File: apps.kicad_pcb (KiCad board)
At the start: 2 copper layers, 100 x 36 mm, 68 parts, among them J1 1-776280-1, J2 SWD, J3 UART, J4 Conn_01x04, Q1 AO3400A, U1 STM32F103C8Tx, U2 MCP2551, U3 AMS1117-5.0, U4 AMS1117-3.3, U5 SS49E, U6 SS49E, Y1 8M

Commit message: Changed SS49E footprint and updated to KiCAD 9
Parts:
- U5, U6: footprint Package_TO_SOT_THT:TO-92_Inline -> SS49E:SS49E_TO_92_Inline
- moved R11 4.00 mm to (191.5, 50.8)
- moved R9 4.00 mm to (195.5, 76.0)
- moved C17 2.50 mm to (192.2, 76.7), turned to 0 degrees
- moved C19 2.46 mm to (194.7, 50.0), turned to 180 degrees
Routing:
- net /Hall Right/OUT: track 29.9 -> 25.8 mm
- net /Hall Left/OUT: track 36.5 -> 40.5 mm
- net GND: track 117.2 -> 117.0 mm, vias 26 -> 28

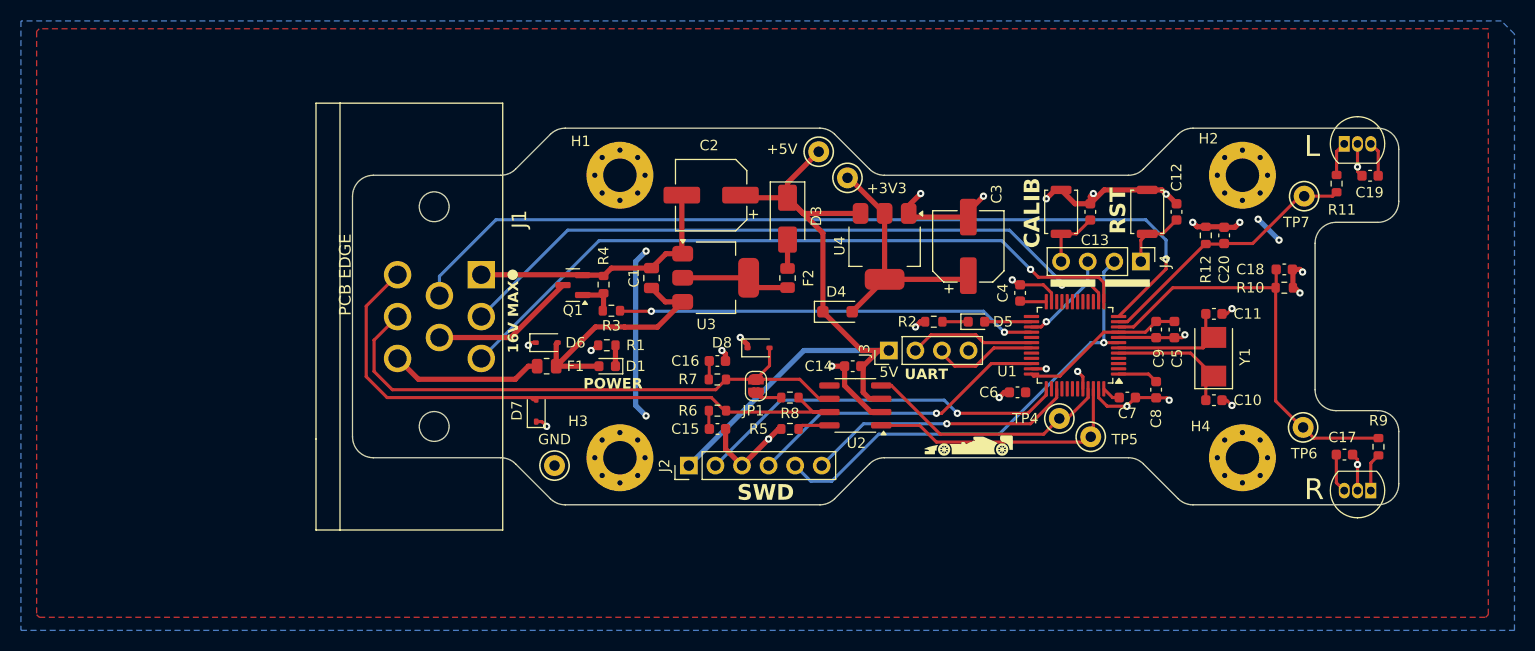
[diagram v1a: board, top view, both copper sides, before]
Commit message: Updated CAN Transceiver and LDO
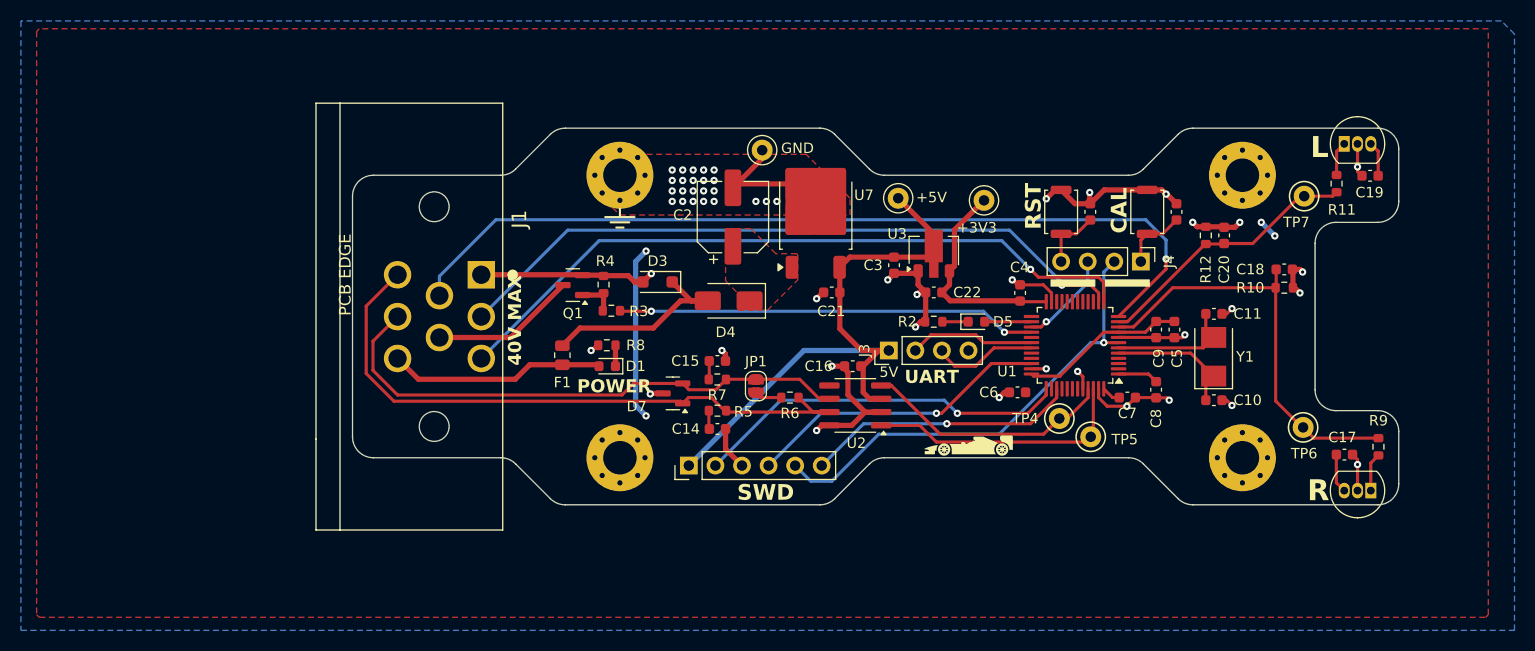
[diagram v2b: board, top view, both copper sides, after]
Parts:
- removed +3V3, +5V, GND: TestPoint, TestPoint:TestPoint_Keystone_5000-5004_Miniature
- removed C1: 4u7, Capacitor_SMD:C_0805_2012Metric
- removed D6, D8: UDD32C12L01-ES, Diode_SMD:D_SOD-323
- removed F2: Polyfuse, Resistor_SMD:R_0805_2012Metric
- removed the R5 at (139.2, 74.2)
- removed U4: AMS1117-3.3, Package_TO_SOT_SMD:SOT-223-3_TabPin2
- added C21: 1u, Capacitor_SMD:C_0603_1608Metric, F.Cu at (143.2, 61.2)
- added C22: 1u, Capacitor_SMD:C_0603_1608Metric, F.Cu at (153.0, 61.2)
- added TP2: TestPoint, TestPoint:TestPoint_Keystone_5000-5004_Miniature, F.Cu at (149.6, 52.2)
- added TP3: TestPoint, TestPoint:TestPoint_Keystone_5000-5004_Miniature, F.Cu at (157.8, 52.4)
- added TP8: TestPoint, TestPoint:TestPoint_Keystone_5000-5004_Miniature, F.Cu at (136.6, 47.6)
- added U7: TPS7B88-Q1, Package_TO_SOT_SMD:TO-252-2, F.Cu at (141.7, 53.8)
- C3: value 10u -> 1u; footprint Capacitor_SMD:CP_Elec_6.3x5.4 -> Capacitor_SMD:C_0603_1608Metric
- D3: value SS34 -> 1N4007; footprint Diode_SMD:D_SMA -> Diode_SMD:D_SOD-123F
- D4: value 1N4007 -> SS34; footprint Diode_SMD:D_SOD-123F -> Diode_SMD:D_SMA
- D7: value UDD32C12L01-ES -> PESD2CAN; footprint Diode_SMD:D_SOD-323 -> Package_TO_SOT_SMD:SOT-23
- SW1: renamed from  RST 
- U2: value MCP2551 -> SN65HVD1050D
- U3: value AMS1117-5.0 -> MCP1700x-500xxMB; footprint Package_TO_SOT_SMD:SOT-223-3_TabPin2 -> Package_TO_SOT_SMD:SOT-89-3
- moved U3 21.0 mm to (153.0, 57.2), turned to 90 degrees
- moved D3 13.8 mm to (126.6, 60.2), turned to 180 degrees
- moved D7 13.2 mm to (128.1, 70.8), turned to 180 degrees
- moved D4 10.5 mm to (133.4, 62.0), turned to 180 degrees
- moved C3 7.32 mm to (149.2, 58.6), turned to -90 degrees
- moved C2 2.96 mm to (133.8, 54.0), turned to 90 degrees
- moved F1 1.83 mm to (117.5, 67.2), turned to 90 degrees
- moved G*** 0.80 mm to (136.0, 62.8)
- renumbered C15 to C14, C16 to C15, C14 to C16, R6 to R5, R8 to R6, R1 to R8, CALIB to SW2
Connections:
- C2 pad 1: +5V -> Net-(D4-K)
- C3 pad 1: +3V3 -> +5V
- D3 pad 1: +5V -> Net-(D3-K)
- D3 pad 2: Net-(D2-A2) -> GND
- D4 pad 1: +5V -> Net-(D4-K)
- D4 pad 2: +3V3 -> Net-(D3-K)
- D7 pad 1: GND -> CANH
- D7 pad 2: CANH -> CANL
- F1 pad 1: Net-(F1-Pad1) -> +12V
- F1 pad 2: +12V -> Net-(D3-K)
- J1 pad 8: Net-(F1-Pad1) -> +12V
- U2 pad 8: Net-(U2-Rs) -> GND
- U3 pad 2: Net-(U3-VO) -> +5V
- U3 pad 3: +12V -> +3V3
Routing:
- net Net-(D3-K): track 0.00 -> 19.8 mm
- net Net-(F1-Pad1): track 14.7 -> 0.00 mm
- net Net-(U3-VO): track 10.4 -> 0.00 mm
- net +5V: track 69.2 -> 61.6 mm
- net +3V3: track 74.1 -> 67.9 mm
- net +12V: track 24.6 -> 20.7 mm
- net Net-(U2-Rs): track 3.09 -> 0.00 mm
- net Net-(D2-A2): track 2.76 -> 0.00 mm
- net CANL: track 55.1 -> 52.6 mm
- net GND: track 117.0 -> 117.8 mm, vias 28 -> 51
- added copper zone on F.Cu, net GND
- added copper zone on F.Cu, net Net-(D4-K)
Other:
- board text added: "+3V3"
- board text added: "+5V"
- board text added: "40V MAX"
- board text added: "CAL"
- board text added: "REV B"
- board text added: "RST"
- board text removed: "16V MAX"
- board text removed: "REV A"
